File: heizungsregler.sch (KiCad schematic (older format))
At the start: 5 parts, among them J101 RPi_GPIO

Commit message: Mbus hinzugefügt
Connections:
- net labels added: RXD, TXD
- wire segments 35 -> 39
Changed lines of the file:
@@
 EESchema Schematic File Version 4
+LIBS:heizungsregler-cache
 EELAYER 26 0
 EELAYER END
 $Descr A4 11693 8268
 encoding utf-8
-Sheet 1 2
+Sheet 1 3
 Title ""
 Date ""
@@
 	4300 3650 5100 3650
 Wire Wire Line
-	5050 3750 4300 3750
+	4300 3750 5100 3750
+$Sheet
+S 6850 3800 550  550
+U 5C09DCA6
+F0 "M-Bus" 50
+F1 "mbus.sch" 50
+F2 "TXD" I L 6850 4000 50
+F3 "RXD" O L 6850 4150 50
+$EndSheet
+Wire Wire Line
+	4300 2150 4950 2150
+Text Label 4950 2150 2    50   ~ 0
+TXD
+Text Label 4950 2250 2    50   ~ 0
+RXD
+Wire Wire Line
+	4950 2250 4300 2250
+Text Label 6600 4000 0    50   ~ 0
+TXD
+Text Label 6600 4150 0    50   ~ 0
+RXD
+Wire Wire Line
+	6600 4000 6850 4000
+Wire Wire Line
+	6600 4150 6850 4150
 $EndSCHEMATC

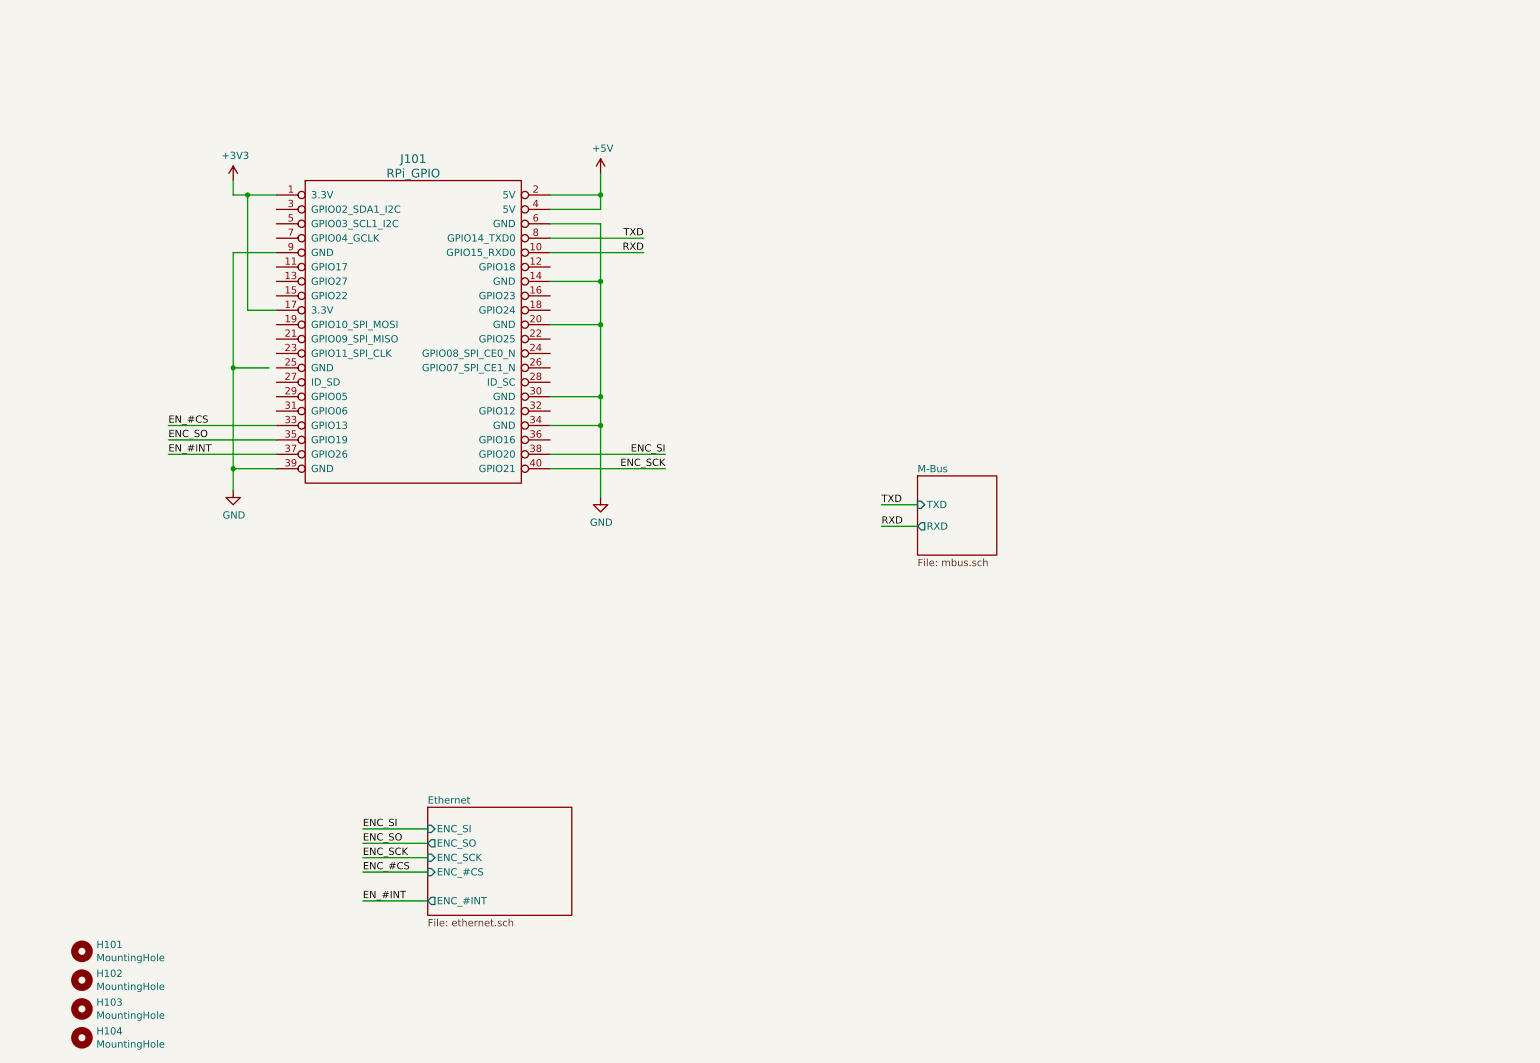
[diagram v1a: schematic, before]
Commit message: Schaltplan weitergemacht, Footprints zugeordnet
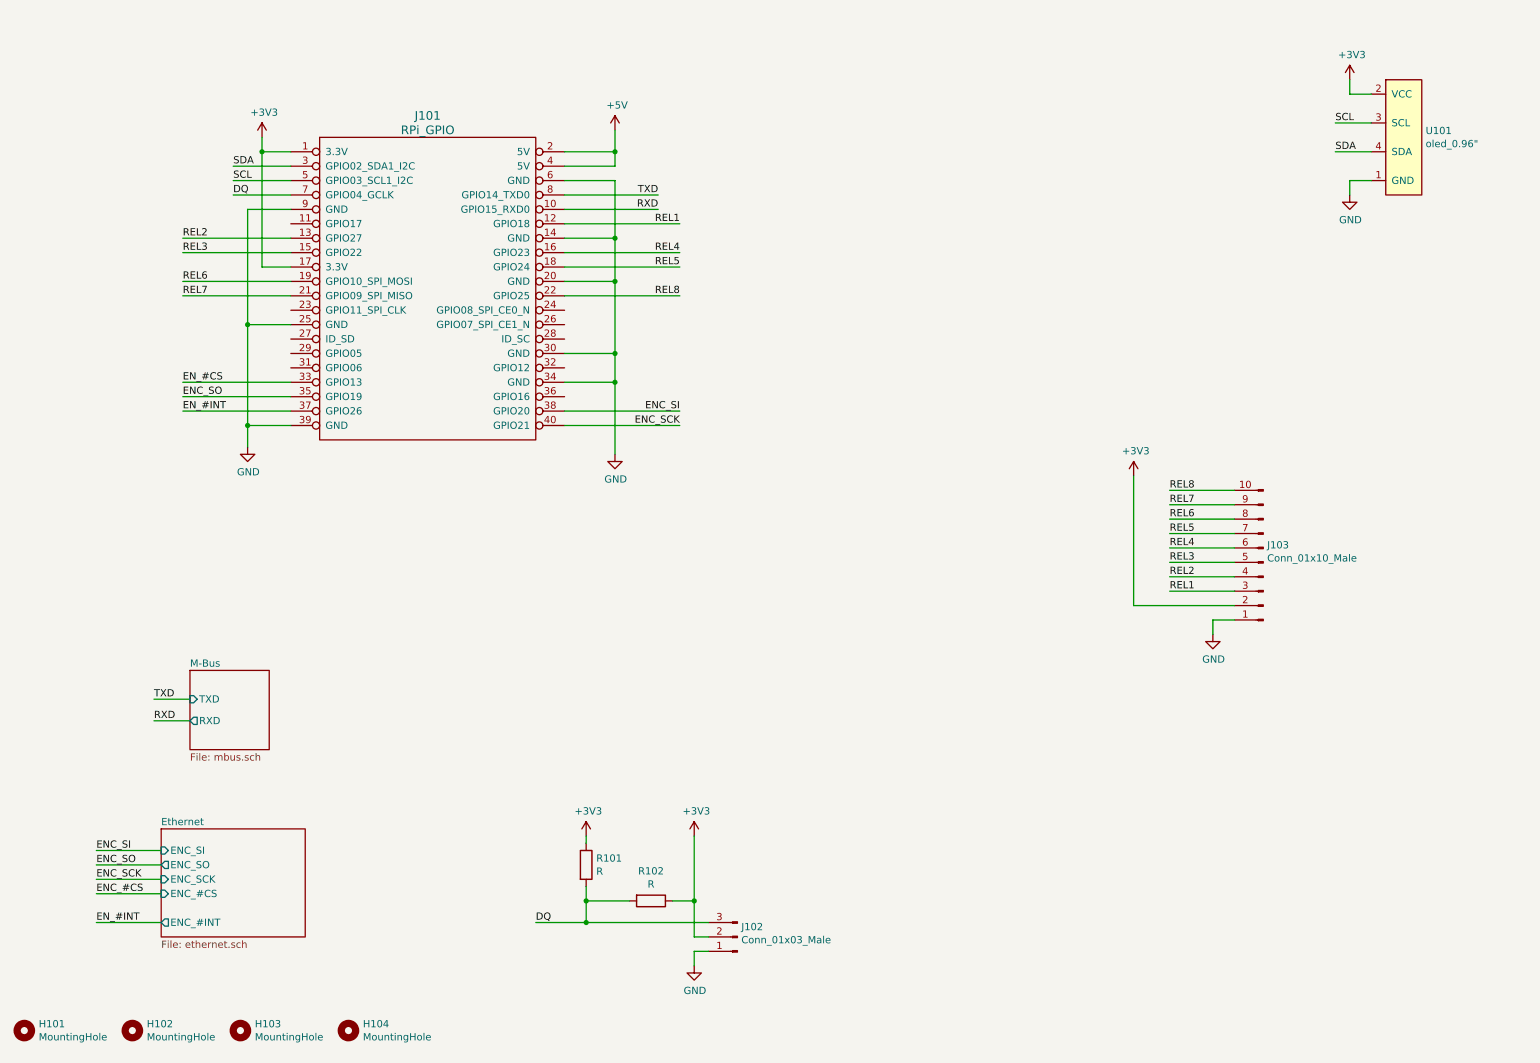
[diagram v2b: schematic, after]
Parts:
- added J102: Conn_01x03_Male, Connector_PinHeader_2.54mm:PinHeader_1x03_P2.54mm_Vertical, symbol Connector:Conn_01x03_Male
- added J103: Conn_01x10_Male, Connector_PinHeader_2.54mm:PinHeader_1x10_P2.54mm_Vertical, symbol Connector:Conn_01x10_Male
- added R101, R102: R, Resistor_SMD:R_0603_1608Metric, symbol Device:R
- added U101: oled_0.96\", kicadlibs:oled_0.96, symbol christof:oled_0.96"
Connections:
- net +3V3: now also J102.2 (Pin_2), J103.2 (Pin_2), R101.1, R102.1, U101.2 (VCC)
- net GND: now also J101.25 (GND), J102.1 (Pin_1), J103.1 (Pin_1), U101.1 (GND)
- net REL1: now reaches J101.12 (GPIO18)
- net REL1: now also J103.3 (Pin_3)
- net REL2: now reaches J101.13 (GPIO27)
- net REL2: now also J103.4 (Pin_4)
- net REL3: now reaches J101.15 (GPIO22)
- net REL3: now also J103.5 (Pin_5)
- net REL4: now reaches J101.16 (GPIO23)
- net REL4: now also J103.6 (Pin_6)
- net REL5: now reaches J101.18 (GPIO24)
- net REL5: now also J103.7 (Pin_7)
- net REL6: now reaches J101.19 (GPIO10_SPI_MOSI)
- net REL6: now also J103.8 (Pin_8)
- net REL7: now reaches J101.21 (GPIO09_SPI_MISO)
- net REL7: now also J103.9 (Pin_9)
- net REL8: now reaches J101.22 (GPIO25)
- net REL8: now also J103.10 (Pin_10)
- net SDA: now reaches J101.3 (GPIO02_SDA1_I2C)
- net SDA: now also U101.4 (SDA)
- net SCL: now reaches J101.5 (GPIO03_SCL1_I2C)
- net SCL: now also U101.3 (SCL)
- net DQ: now reaches J101.7 (GPIO04_GCLK)
- net DQ: now also J102.3 (Pin_3), R101.2, R102.2
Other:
- moved on the sheet: H101, H102, H103, H104, J101

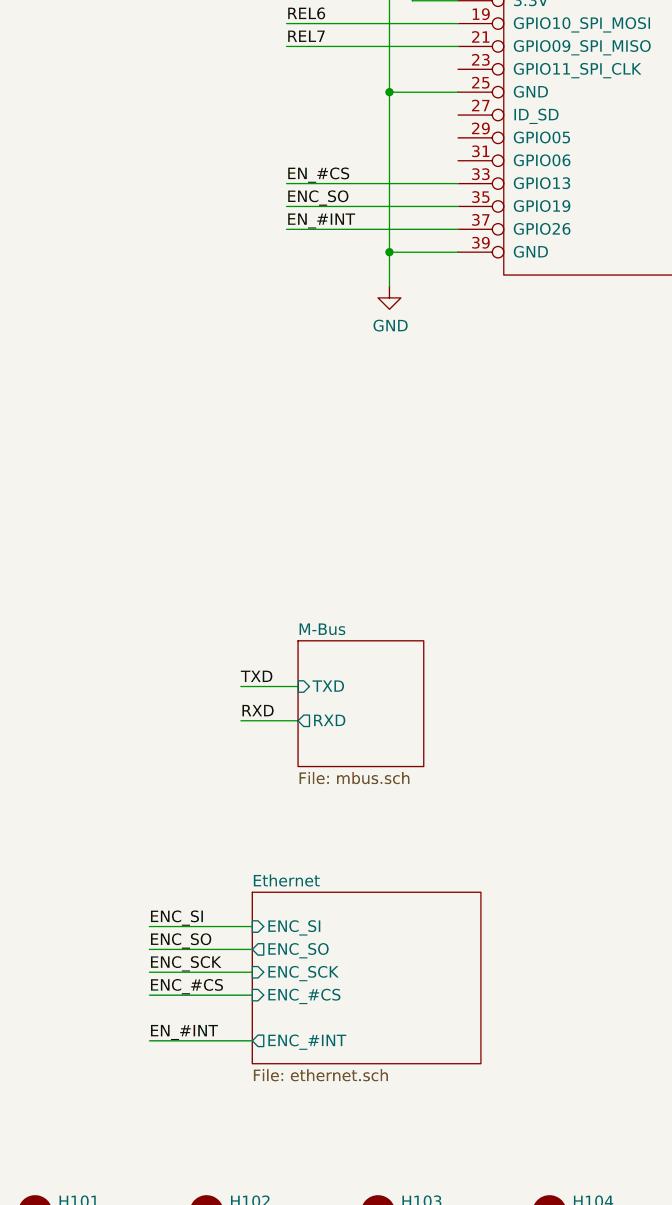
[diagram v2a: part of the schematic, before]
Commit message: Platzierung begonnen, Signalnamen ENC korrigiert
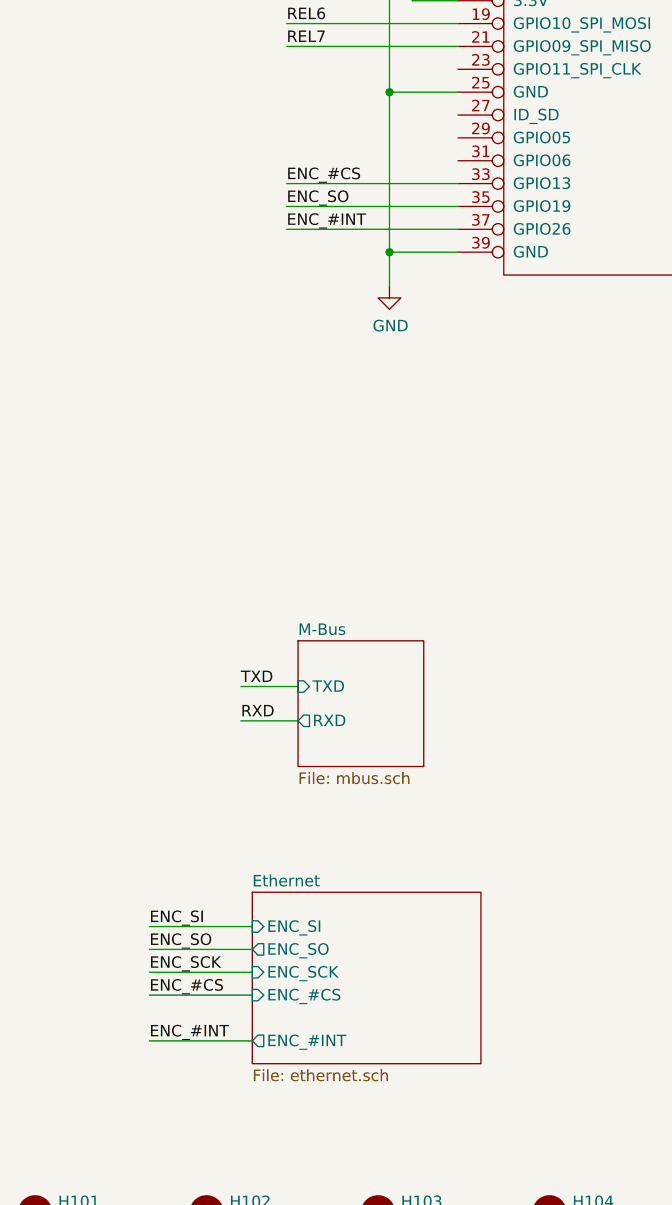
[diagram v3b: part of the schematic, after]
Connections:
- net EN_#CS is gone; now on net ENC_#CS: J101.33 (GPIO13)
- net EN_#INT renamed ENC_#INT
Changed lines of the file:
@@
 	4400 3150 4750 3150
 Text Label 1750 3150 0    50   ~ 0
-EN_#CS
+ENC_#CS
 Wire Wire Line
 	1750 3150 2500 3150
@@
 ENC_#CS
 Text Label 1150 6900 0    50   ~ 0
-EN_#INT
+ENC_#INT
 Text Label 1750 3350 0    50   ~ 0
-EN_#INT
+ENC_#INT
 Wire Wire Line
 	1750 3350 2500 3350

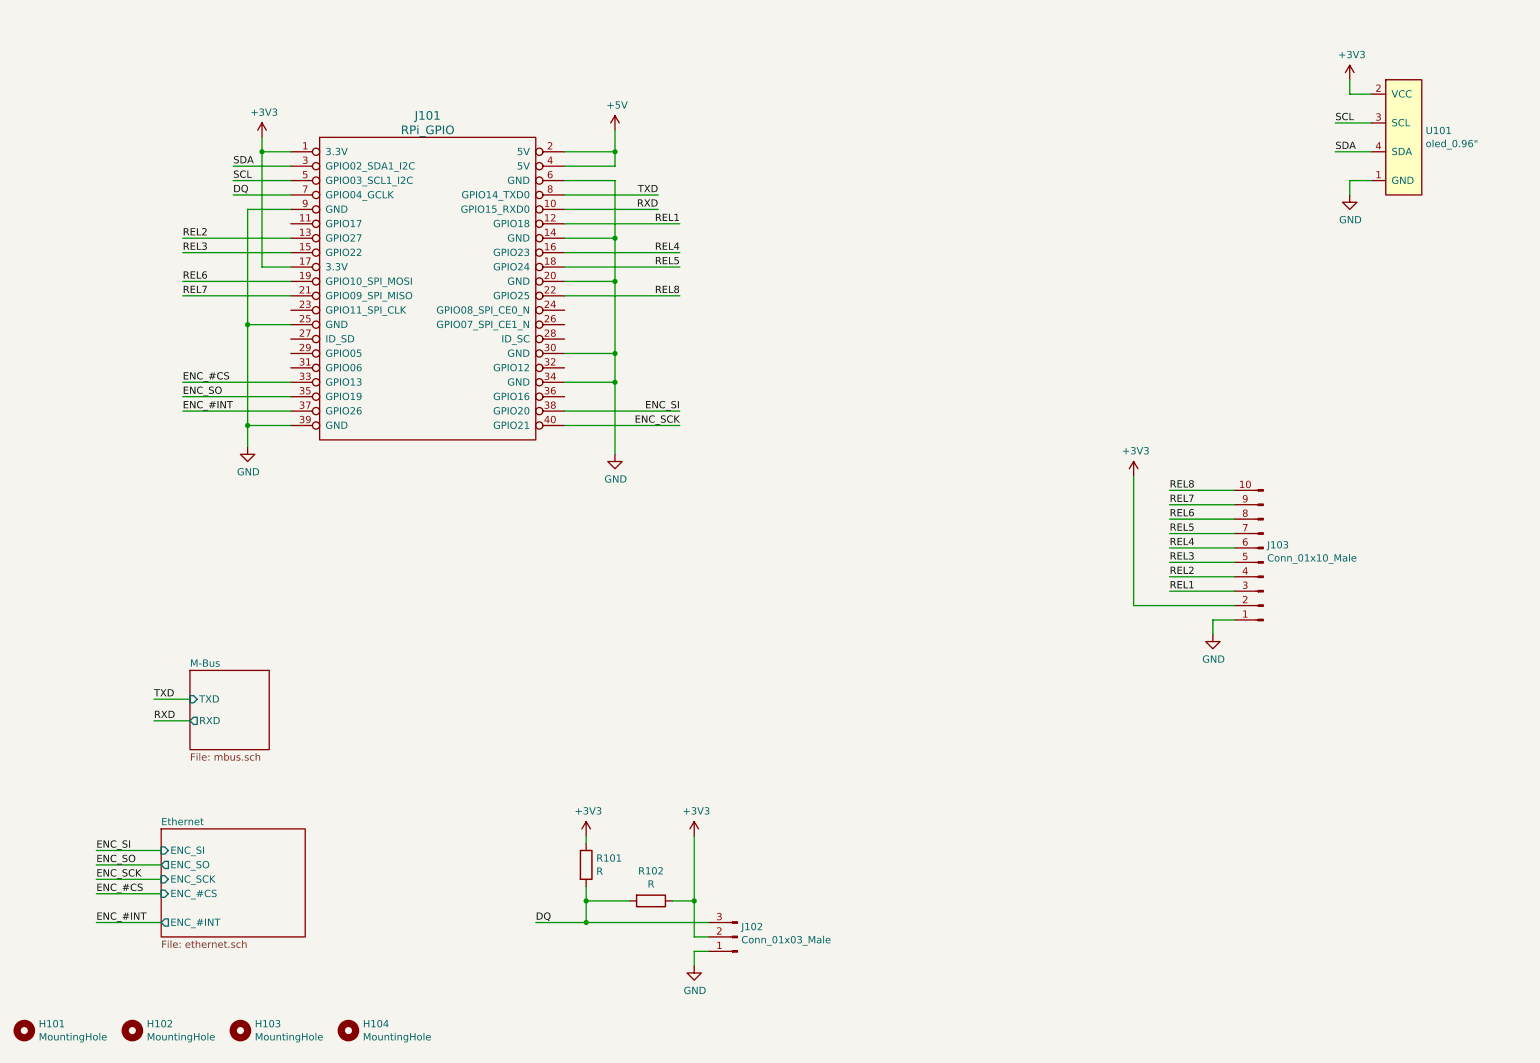
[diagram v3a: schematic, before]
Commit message: ENC28J60 platziert und geroutet
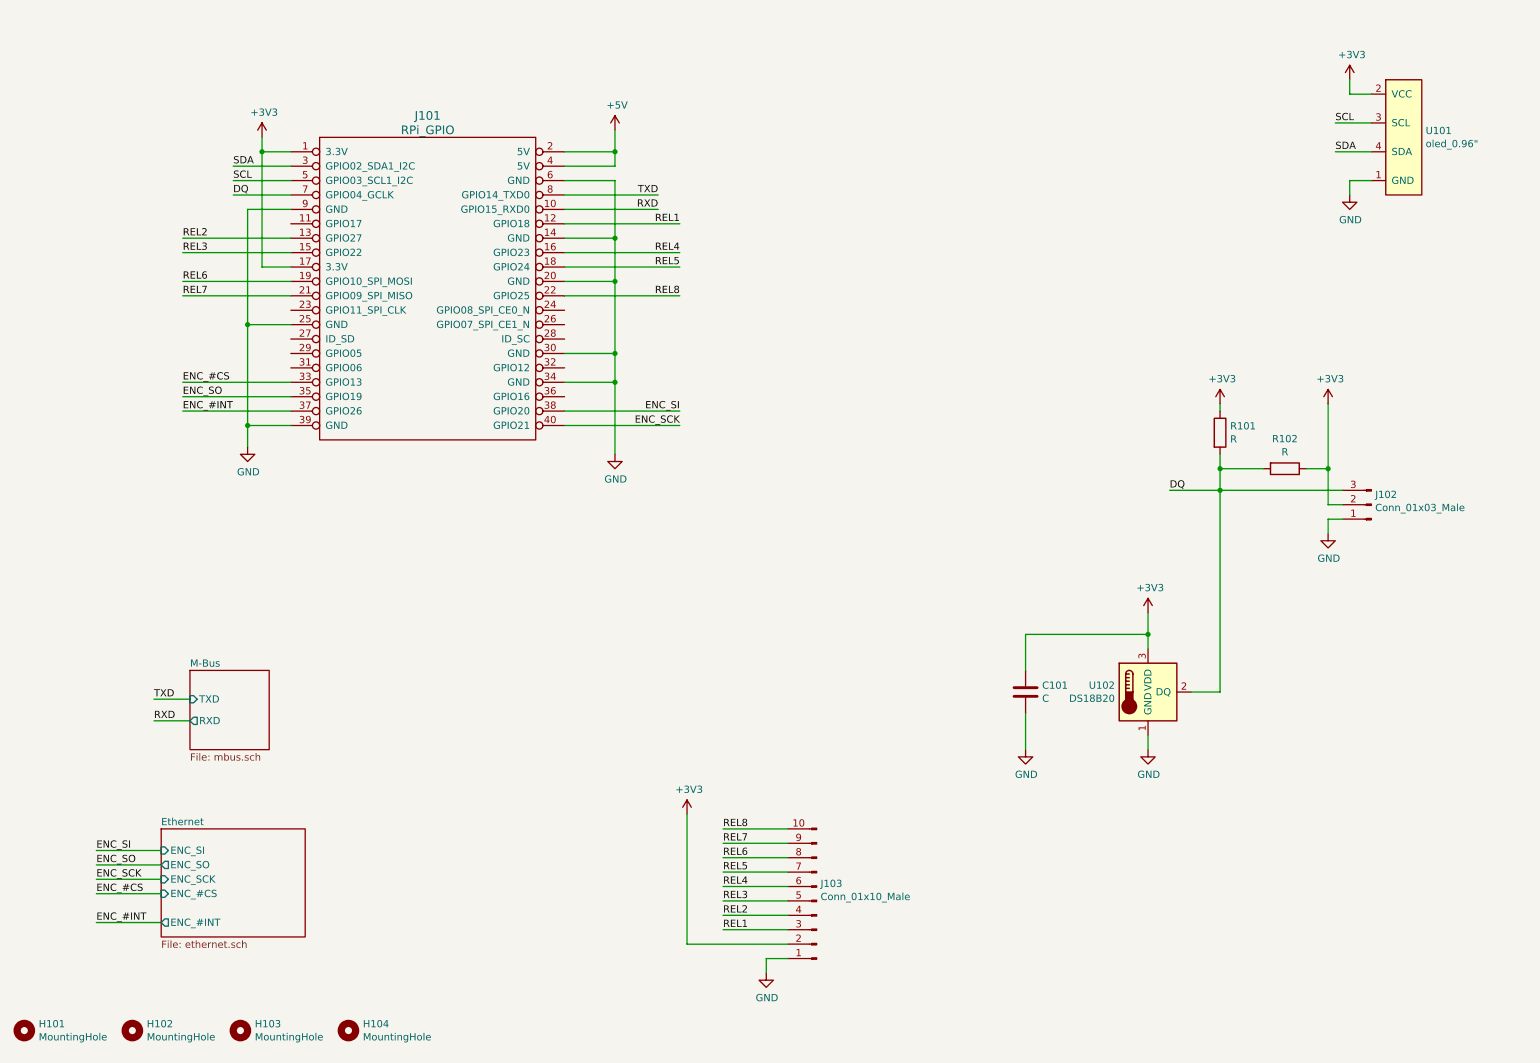
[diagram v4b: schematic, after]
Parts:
- added C101: C, Capacitor_SMD:C_0603_1608Metric, symbol Device:C
- added U102: DS18B20, Package_TO_SOT_THT:TO-92_Inline, symbol Sensor_Temperature:DS18B20
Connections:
- net +3V3: now also C101.1, U102.3 (VDD)
- net DQ: now also U102.2 (DQ)
- net GND: now also C101.2, U102.1 (GND)
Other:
- moved on the sheet: J102, J103, R101, R102

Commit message: Noch mehr Layout
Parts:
- removed R102: R, Resistor_SMD:R_0603_1608Metric, symbol Device:R
- added H105, H106, H107, H108: MountingHole, MountingHole:MountingHole_3.2mm_M3_DIN965_Pad, symbol Mechanical:MountingHole
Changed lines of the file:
@@
 	1    0    0    -1
 $EndComp
-Wire Wire Line
-	9700 3300 9700 3750
-$Comp
-L Device:R R102
-U 1 1 5C10BD5A
-P 9400 3750
-F 0 "R102" V 9193 3750 50  0000 C CNN
-F 1 "R" V 9284 3750 50  0000 C CNN
-F 2 "Resistor_SMD:R_0603_1608Metric" V 9330 3750 50  0001 C CNN
-F 3 "~" H 9400 3750 50  0001 C CNN
-	1    9400 3750
-	0    1    1    0
-$EndComp
-Wire Wire Line
-	9700 3750 9550 3750
-Connection ~ 9700 3750
-Wire Wire Line
-	9700 3750 9700 4000
 Text Label 2100 1850 0    50   ~ 0
 DQ
@@
 Connection ~ 8950 3900
 Wire Wire Line
-	8950 3650 8950 3750
-Connection ~ 8950 3750
-Wire Wire Line
-	8950 3750 8950 3900
-Wire Wire Line
-	8950 3750 9250 3750
-Wire Wire Line
 	8950 3900 9800 3900
 $Comp
@@
 Wire Wire Line
 	8950 5300 8950 3900
+$Comp
+L Mechanical:MountingHole H105
+U 1 1 5C0FF546
+P 650 7400
+F 0 "H105" H 750 7446 50  0000 L CNN
+F 1 "MountingHole" H 750 7355 50  0000 L CNN
+F 2 "MountingHole:MountingHole_3.2mm_M3_DIN965_Pad" H 650 7400 50  0001 C CNN
+F 3 "~" H 650 7400 50  0001 C CNN
+	1    650  7400
+	1    0    0    -1
+$EndComp
+$Comp
+L Mechanical:MountingHole H106
+U 1 1 5C0FF54D
+P 1400 7400
+F 0 "H106" H 1500 7446 50  0000 L CNN
+F 1 "MountingHole" H 1500 7355 50  0000 L CNN
+F 2 "MountingHole:MountingHole_3.2mm_M3_DIN965_Pad" H 1400 7400 50  0001 C CNN
+F 3 "~" H 1400 7400 50  0001 C CNN
+	1    1400 7400
+	1    0    0    -1
+$EndComp
+$Comp
+L Mechanical:MountingHole H107
+U 1 1 5C0FF554
+P 2150 7400
+F 0 "H107" H 2250 7446 50  0000 L CNN
+F 1 "MountingHole" H 2250 7355 50  0000 L CNN
+F 2 "MountingHole:MountingHole_3.2mm_M3_DIN965_Pad" H 2150 7400 50  0001 C CNN
+F 3 "~" H 2150 7400 50  0001 C CNN
+	1    2150 7400
+	1    0    0    -1
+$EndComp
+$Comp
+L Mechanical:MountingHole H108
+U 1 1 5C0FF55B
+P 2900 7400
+F 0 "H108" H 3000 7446 50  0000 L CNN
+F 1 "MountingHole" H 3000 7355 50  0000 L CNN
+F 2 "MountingHole:MountingHole_3.2mm_M3_DIN965_Pad" H 2900 7400 50  0001 C CNN
+F 3 "~" H 2900 7400 50  0001 C CNN
+	1    2900 7400
+	1    0    0    -1
+$EndComp
+Wire Wire Line
+	9700 3300 9700 4000
+Wire Wire Line
+	8950 3650 8950 3900
 $EndSCHEMATC
